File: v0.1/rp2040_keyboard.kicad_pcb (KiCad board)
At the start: 2 copper layers, 86.2 x 70.2 mm, 56 parts, among them J1 USB_C_Receptacle_USB2.0, SW1 KEY_1_00, SW10 KEY_10_21, SW11 KEY_11_22, SW12 KEY_12_23, SW13 SW_SPDT, SW2 KEY_2_01, SW3 KEY_3_02, SW4 KEY_4_03, SW5 KEY_5_10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

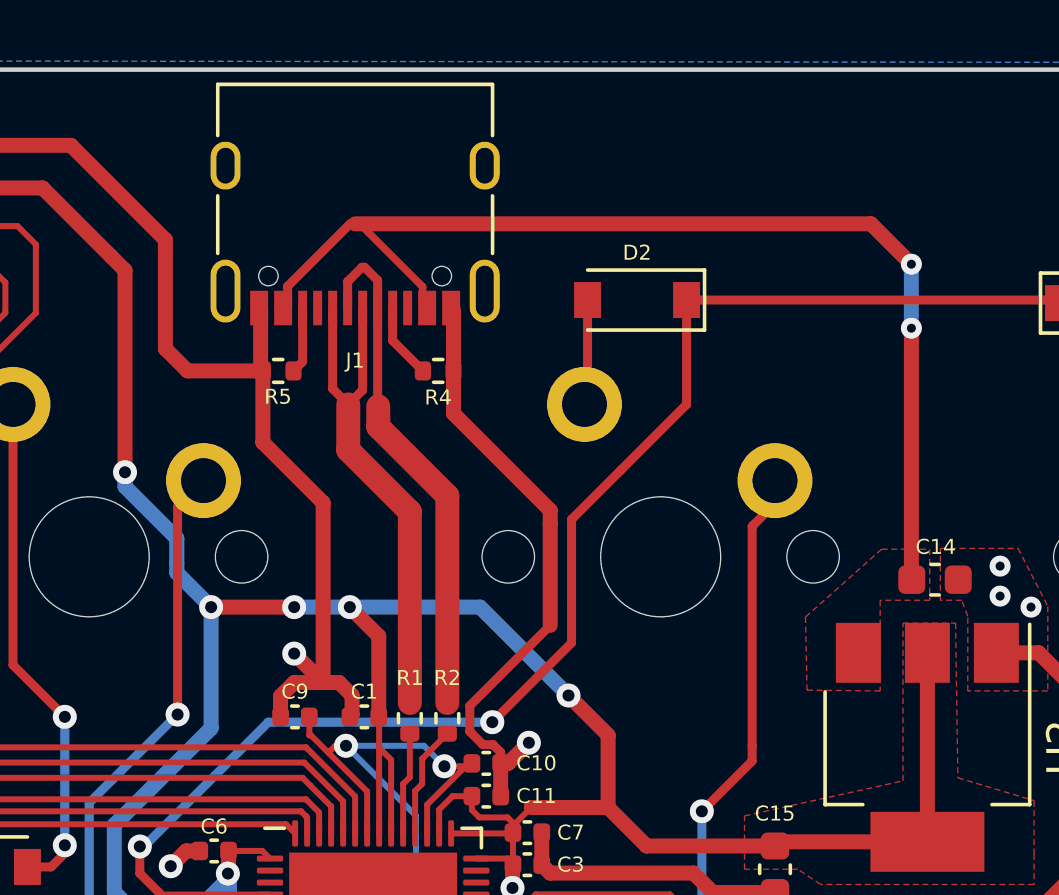
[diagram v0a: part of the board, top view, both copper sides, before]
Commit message: center of usb c port
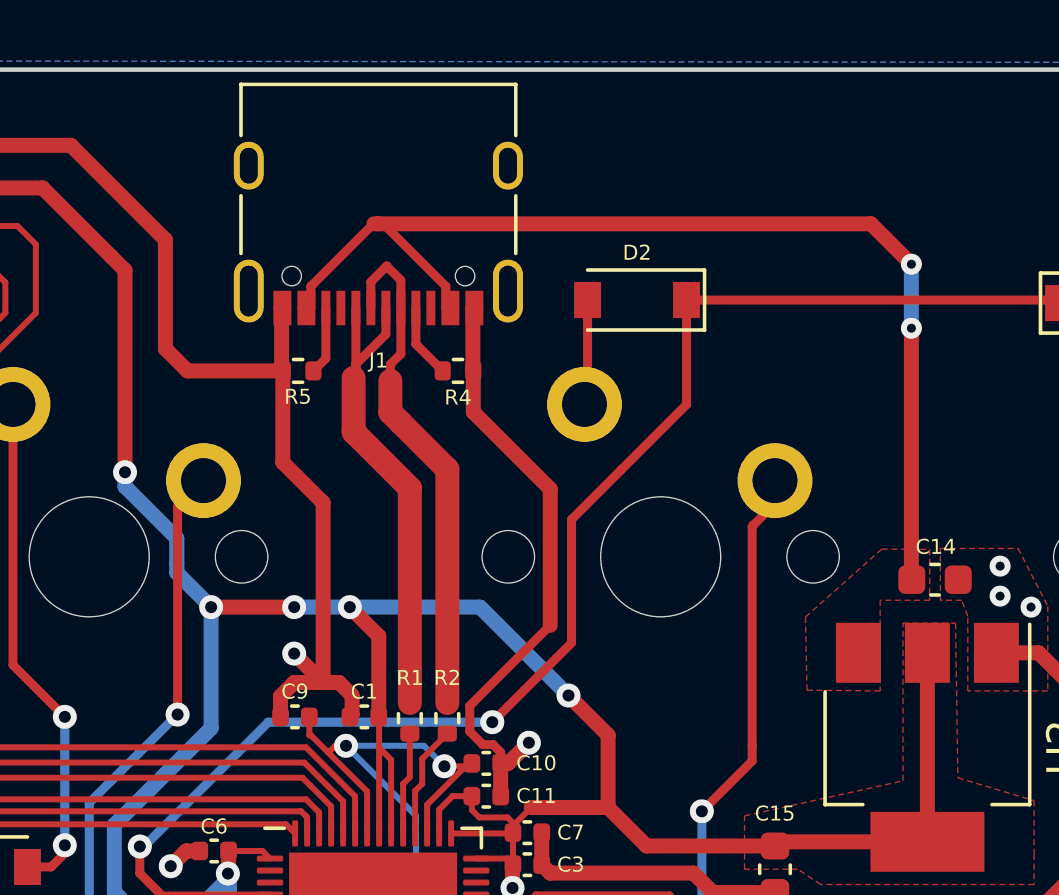
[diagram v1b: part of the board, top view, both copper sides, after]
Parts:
- moved J1 0.78 mm to (88.1, 47.7)
- moved R5 0.66 mm to (85.5, 53.5)
- moved R4 0.66 mm to (90.8, 53.5)
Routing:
- net /USB_D+: track 17.6 -> 16.4 mm
- net VBUS: track 37.9 -> 37.1 mm
